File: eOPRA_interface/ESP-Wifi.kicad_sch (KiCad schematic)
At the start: 18 parts, among them SW1 SW_Push

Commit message: stuff
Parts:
- removed C33: 1uF, 2_Passives_Resistors_SMD_IPC:R_1005_402_A, symbol 2.passive:C
- removed D3: LED, 1_Semi_Discrete_Diodes_SMD:D_0603, symbol 1.semi.opto:LED
- removed R4: 500, 2_Passives_Resistors_SMD_IPC:R_1608_603_B, symbol 2.passive:R
- removed TP10, TP13: TEST, 0_misc:test_point_1.0mm_square, symbol 5.connector.interconnect:TEST
- added D3 (x3): LED, 1_Semi_Discrete_Diodes_SMD:D_0603, symbol 1.semi.opto:LED
- added JP2, JP3: ~, 0_misc:SolderJumper-2_P1.3mm_Bridged_RoundedPad1.0x1.5mm, symbol 2.passive:Jumper_NC_Small
- added Q7 (x2): Q_NMOS_GSD, 1_Semi_TO_SOT:SOT-323FL, symbol 1.semi.discrete:Q_NMOS_GSD
- added R16 (x2): 300, 2_Passives_Resistors_SMD_IPC:R_1608_603_B, symbol 2.passive:R
- added R25 (x4), R49 (x2): 10k, 2_Passives_Resistors_SMD_IPC:R_1608_603_B, symbol 2.passive:R
- added TP3: TEST, 0_misc:test_point_1.0mm_square, symbol 5.connector.interconnect:TEST
- C33: footprint 2_Passives_Resistors_SMD_IPC:R_1005_402_A -> 2_Passives_Capacitors_SMD_IPC:C_1005_402_A; PN (none) -> 2,2
- R25: PN (none) -> 1,2
- SW1: PN (none) -> 9,4
- U16: PN (none) -> 5,4
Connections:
- net +3V3: now also D3.2 (A), D3.2 (A), D3.2 (A), R25.1, R25.1
- net EN: now also R25.2; no longer R25.2, SW1.1, SW1.3
- net ESP_INT: now also U16.5 (IO14); no longer U16.19 (IO4)
- net GND: now also Q7.2 (S), Q7.2 (S), R25.2, R49.1, R49.1
- net GPIO0: now also TP9.1, R25.2
- net SCL1: now also JP2.1; no longer U16.5 (IO14)
- net SDA1: now also JP3.1; no longer U16.17 (IO2)
- net ~{RESET}: now reaches U16.1 (RESET)
- net ~{RESET}: now also R25.2, SW1.1, SW1.3
- net GPIO2: now reaches TP1.1
- net GPIO2: now also U16.17 (IO2), R25.2; no longer U16.7 (IO13)
- net at U16.16 (IO15): now also R25.1
- net at U16.20 (IO5): now also JP2.2
- net LED1: now reaches U16.6 (IO12)
- net LED1: now also R16.2, R49.2; no longer TP9.1
- net LED_STATIC: no longer names the net of U16.4 (IO16)
- net LED_STATIC: now also TP3.1
- new net: D3.1 (K), Q7.3 (D) (x2)
- new net: D3.1 (K), R25.1
- new net: Q7.1 (G), R16.1 (x2)
- new net: JP3.2, U16.19 (IO4)
- new net LED2: R16.2, R49.2, U16.7 (IO13)
- no-connect marks 2 -> 1
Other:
- note added: "(GPIO pins output 12mA only)"
- moved on the sheet: C33, R25, SW1, TP11, TP12, TP5, TP6, TP7, TP8, U16

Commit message: stuff
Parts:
- removed Q7 (x2): Q_NMOS_GSD, 1_Semi_TO_SOT:SOT-323FL, symbol 1.semi.discrete:Q_NMOS_GSD
- removed R16 (x2): 300, 2_Passives_Resistors_SMD_IPC:R_1608_603_B, symbol 2.passive:R
- removed R49 (x2): 10k, 2_Passives_Resistors_SMD_IPC:R_1608_603_B, symbol 2.passive:R
- added R80 (x2): 120, 2_Passives_Resistors_SMD_IPC:R_1005_402_A, symbol 2.passive:R
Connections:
- net +3V3: no longer D3.2 (A), D3.2 (A)
- net GND: now also D3.1 (K), D3.1 (K)
- net LED1: now also R80.2
- net LED2: now also R80.2
- new net: D3.2 (A), R80.1 (x2)
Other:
- moved on the sheet: D3

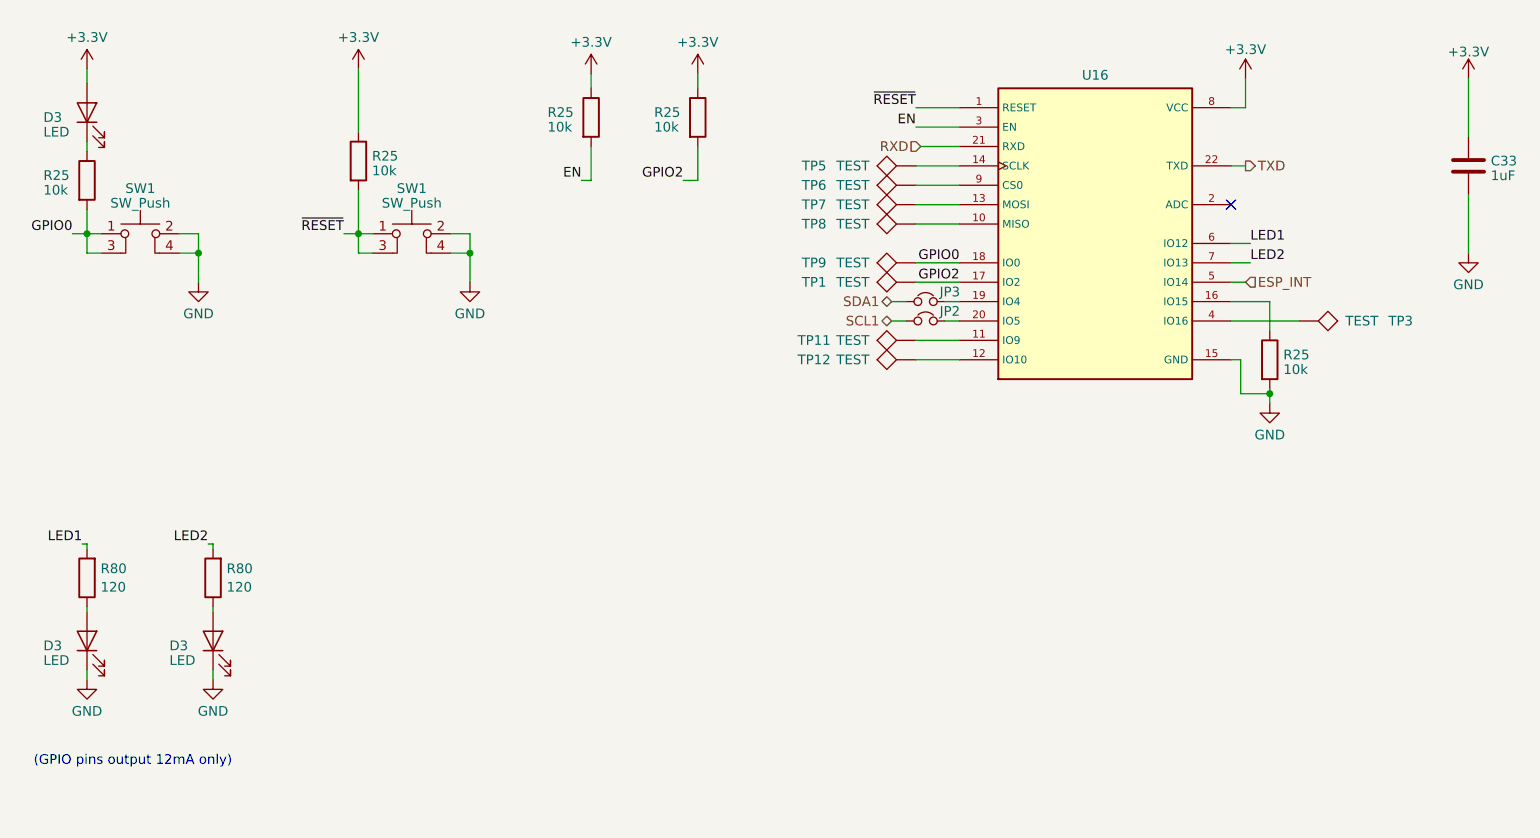
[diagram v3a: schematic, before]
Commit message: switch port on interrupt
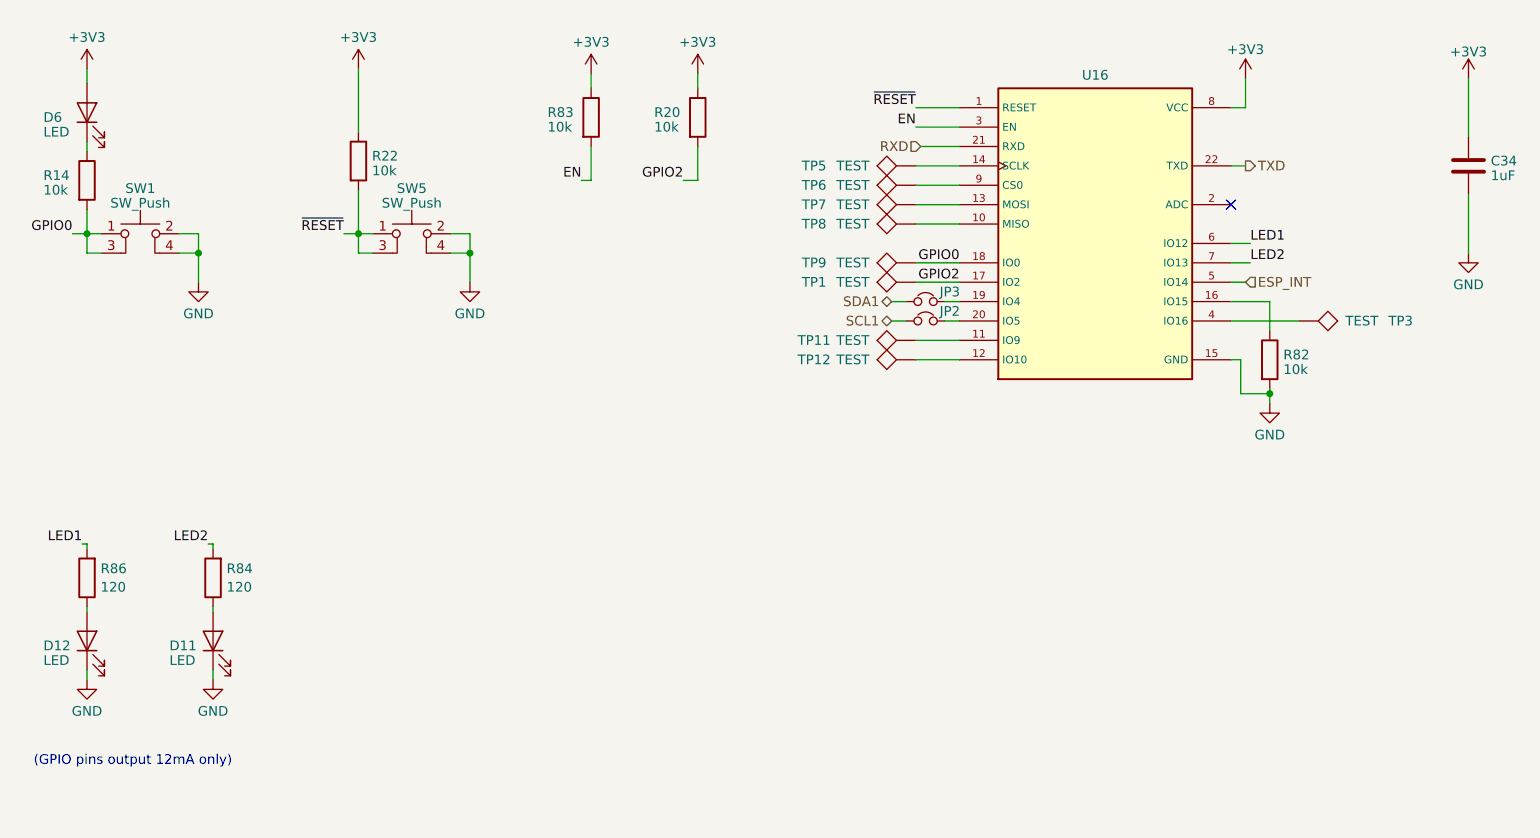
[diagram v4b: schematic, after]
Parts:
- renumbered C33 to C34, D3 to D11, D3 to D12, D3 to D6, R25 to R14, R25 to R20, R25 to R22, R25 to R82, R25 to R83, R80 to R84, R80 to R86, SW1 to SW5
